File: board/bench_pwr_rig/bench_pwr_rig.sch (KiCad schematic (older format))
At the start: 49 parts, among them J1 703W-00_54, K1 G5Q-1A, Q1 Si2319CDS, Q2 BSS138, Q3 STP110N10F7, Q4 STP110N10F7, SW1 SW_SPDT, U1 FODM217B, U2 PEME1-S5-S12-S, U3 LM317_TO-220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

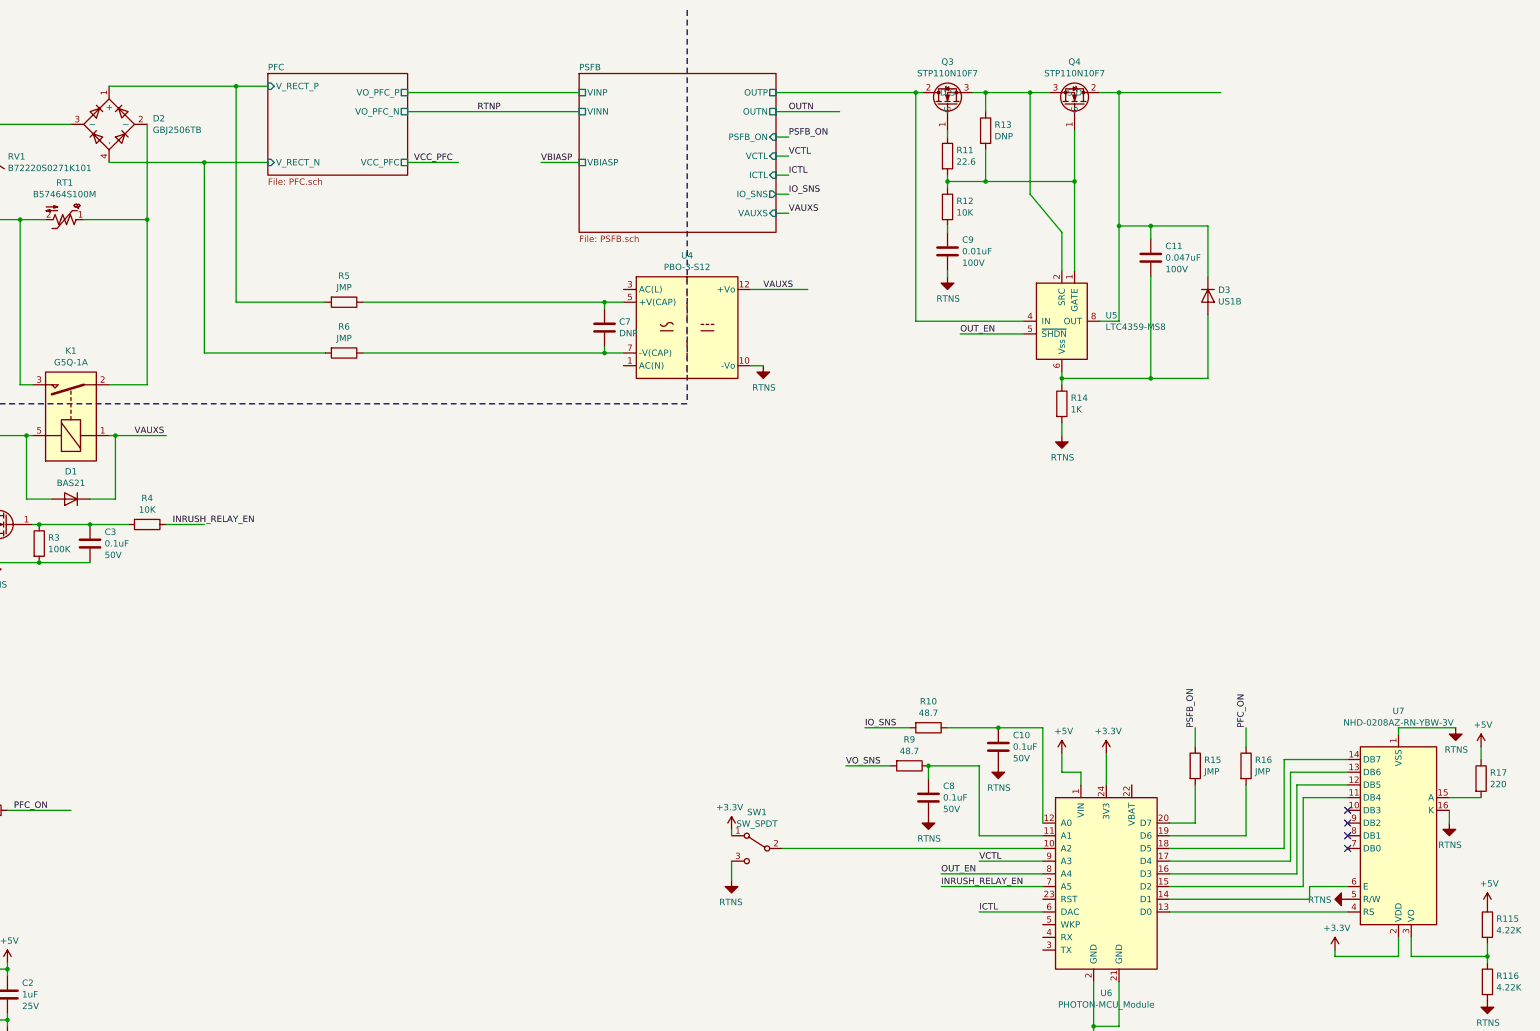
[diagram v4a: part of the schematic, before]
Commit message: Updated layout
Added output screw terminal
Added mounting screws M4
Changed primary ground to secondary ground plane coupling capacitor to radial disc type with safety rating X1, Y1
Continued layout
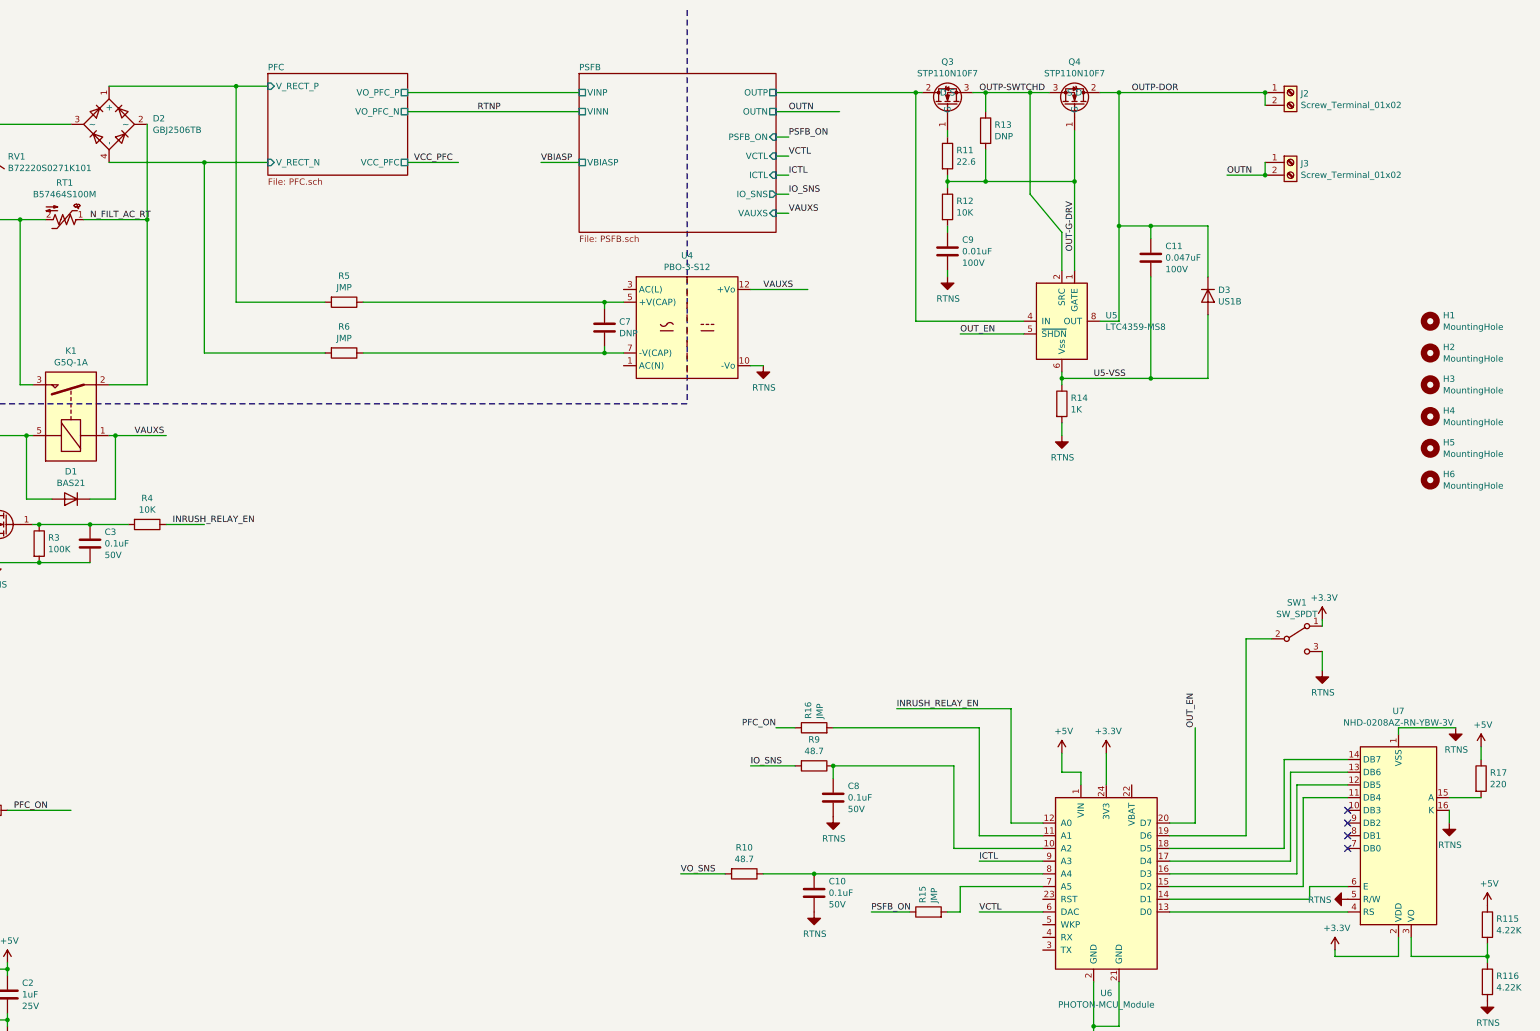
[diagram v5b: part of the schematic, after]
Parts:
- added H1, H2, H3, H4, H5, H6: MountingHole, MountingHole:MountingHole_4.3mm_M4, symbol Mechanical:MountingHole
- added J2, J3: Screw_Terminal_01x02, TerminalBlock_Phoenix:TerminalBlock_Phoenix_MKDS-1,5-2-5.08_1x02_P5.08mm_Horizontal, symbol Connector:Screw_Terminal_01x02
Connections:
- net labels added: N_FILT_AC_RT, OUT-G-DRV, OUTP-DOR, OUTP-SWTCHD, U5-VSS
- wire segments 207 -> 216
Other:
- moved on the sheet: C10, C8, R10, R15, R16, R9, SW1
